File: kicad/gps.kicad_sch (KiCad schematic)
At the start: 61 parts, among them J1 Bus_PCI_Express_x1, J2 USB_C_Receptacle_USB2.0_16P, J3 Conn_01x02, J4 USB_C_Receptacle_USB2.0_16P, U2 W25Q128JVP, U3 MCP25625T-E/ML, U4 RP2040, U5 NEO-M9N, X1 ABM8-272-T3, Y1 X322516MLB4SI

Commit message: Update gps.kicad_pcb
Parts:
- RF1: footprint GPSLIB:SMA-SMD_BWSMA-KE-P001 -> GPSLIB:SMA-TH_BWSMA-KWE-Z001
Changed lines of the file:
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@@
 			)
 		)
-		(property "Footprint" "GPSLIB:SMA-SMD_BWSMA-KE-P001"
+		(property "Footprint" "GPSLIB:SMA-TH_BWSMA-KWE-Z001"
 			(at 316.23 96.52 0)
 			(effects

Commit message: Update footprints
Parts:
- S1, S2: footprint TS-1187A-B-A-B:SW_TS-1187A-B-A-B -> GPSLIB:SW_TS-1187A-B-A-B
- U3: footprint MCP25625T_E_ML:QFN28_6X6MC_MCH -> GPSLIB:QFN28_6X6MC_MCH
- X1: footprint ABM8-272-T3:ABM8-272-T3_ABR -> GPSLIB:ABM8-272-T3_ABR
- Y1: footprint X322516MLB4SI:OSC_X322516MLB4SI -> GPSLIB:OSC_X322516MLB4SI
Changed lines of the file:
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@@
 			)
 		)
-		(property "Footprint" "X322516MLB4SI:OSC_X322516MLB4SI"
+		(property "Footprint" "GPSLIB:OSC_X322516MLB4SI"
 			(at 304.8 231.14 0)
 			(effects
@@
 			)
 		)
-		(property "Footprint" "TS-1187A-B-A-B:SW_TS-1187A-B-A-B"
+		(property "Footprint" "GPSLIB:SW_TS-1187A-B-A-B"
 			(at 48.26 67.31 0)
 			(effects
@@
 			)
 		)
-		(property "Footprint" "ABM8-272-T3:ABM8-272-T3_ABR"
+		(property "Footprint" "GPSLIB:ABM8-272-T3_ABR"
 			(at 45.72 232.41 0)
 			(effects
@@
 			)
 		)
-		(property "Footprint" "MCP25625T_E_ML:QFN28_6X6MC_MCH"
+		(property "Footprint" "GPSLIB:QFN28_6X6MC_MCH"
 			(at 287.02 171.45 0)
 			(effects
@@
 			)
 		)
-		(property "Footprint" "TS-1187A-B-A-B:SW_TS-1187A-B-A-B"
+		(property "Footprint" "GPSLIB:SW_TS-1187A-B-A-B"
 			(at 35.56 189.23 0)
 			(effects

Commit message: wip
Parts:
- added R3, R4: 27, Resistor_SMD:R_0402_1005Metric, symbol Device:R
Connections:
- net GPS_USB_D+: now also R4.1; no longer U5.6 (USB_DP)
- net GPS_USB_D-: now also R3.1; no longer U5.5 (USB_DM)
- new net: R3.2, U5.5 (USB_DM)
- new net: R4.2, U5.6 (USB_DP)

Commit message: Update pcb
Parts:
- R10, R13: value 150 -> 1k; JLC Link https://jlcpcb.com/partdetail/23535-0603WAF1500T5E/C22808 -> (none); LCSC Part # C22808 -> (none); info 150 ohm -> (none)
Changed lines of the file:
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@@
 			)
 		)
-		(property "Value" "150"
+		(property "Value" "1k"
 			(at 266.446 251.46 0)
 			(effects
@@
 			)
 		)
-		(property "JLC Link" "https://jlcpcb.com/partdetail/23535-0603WAF1500T5E/C22808"
+		(property "JLC Link" ""
 			(at 271.78 250.19 0)
 			(effects
@@
 			)
 		)
-		(property "LCSC Part #" "C22808"
+		(property "LCSC Part #" ""
 			(at 271.78 250.19 0)
 			(effects
@@
 			)
 		)
-		(property "info" "150 ohm"
+		(property "info" ""
 			(at 271.78 250.19 0)
 			(effects
@@
 			)
 		)
-		(property "Value" "150"
+		(property "Value" "1k"
 			(at 253.746 251.46 0)
 			(effects
@@
 			)
 		)
-		(property "JLC Link" "https://jlcpcb.com/partdetail/23535-0603WAF1500T5E/C22808"
+		(property "JLC Link" ""
 			(at 259.08 250.19 0)
 			(effects
@@
 			)
 		)
-		(property "LCSC Part #" "C22808"
+		(property "LCSC Part #" ""
 			(at 259.08 250.19 0)
 			(effects
@@
 			)
 		)
-		(property "info" "150 ohm"
+		(property "info" ""
 			(at 259.08 250.19 0)
 			(effects

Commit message: Update pcb
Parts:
- R20, R22: LCSC Part # C25105 -> (none); info 1000 ohm -> (none)
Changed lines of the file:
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@@
 			)
 		)
-		(property "LCSC Part #" "C25105"
+		(property "LCSC Part #" ""
 			(at 384.81 143.51 0)
 			(effects
@@
 			)
 		)
-		(property "info" "1000 ohm"
+		(property "info" ""
 			(at 384.81 143.51 0)
 			(effects
@@
 			)
 		)
-		(property "LCSC Part #" "C25105"
+		(property "LCSC Part #" ""
 			(at 377.19 143.51 0)
 			(effects
@@
 			)
 		)
-		(property "info" "1000 ohm"
+		(property "info" ""
 			(at 377.19 143.51 0)
 			(effects

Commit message: Update pcb
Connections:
- net +3.3V: now also C22.1, U5.23 (VCC)
- net +3V3: no longer C22.1, U5.23 (VCC)
- net RF_ANT: now reaches L1.2, RF1.5, U5.11 (RF_IN)
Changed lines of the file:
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@@
 		)
 	)
+	(global_label "RF_ANT"
+		(shape input)
+		(at 294.64 96.52 90)
+		(fields_autoplaced yes)
+		(effects
+			(font
+				(size 1.27 1.27)
+			)
+			(justify left)
+		)
+		(property "Intersheetrefs" "${INTERSHEET_REFS}"
+			(at 294.64 86.8219 90)
+			(effects
+				(font
+					(size 1.27 1.27)
+				)
+				(justify left)
+				(hide yes)
+			)
+		)
+	)
 	(global_label "CANSTBY"
 		(shape input)
@@
 	)
 	(symbol
-		(lib_id "power:+3V3")
-		(at 260.35 71.12 0)
-		(unit 1)
-		(exclude_from_sim no)
-		(in_bom yes)
-		(on_board yes)
-		(dnp no)
-		(fields_autoplaced yes)
-		(property "Reference" "#PWR057"
-			(at 260.35 74.93 0)
-			(effects
-				(font
-					(size 1.27 1.27)
-				)
-				(hide yes)
-			)
-		)
-		(property "Value" "+3V3"
-			(at 260.35 66.04 0)
-			(effects
-				(font
-					(size 1.27 1.27)
-				)
-			)
-		)
-		(property "Footprint" ""
-			(at 260.35 71.12 0)
-			(effects
-				(font
-					(size 1.27 1.27)
-				)
-				(hide yes)
-			)
-		)
-		(property "Datasheet" ""
-			(at 260.35 71.12 0)
-			(effects
-				(font
-					(size 1.27 1.27)
-				)
-				(hide yes)
-			)
-		)
-		(property "Description" ""
-			(at 260.35 71.12 0)
-			(effects
-				(font
-					(size 1.27 1.27)
-				)
-				(hide yes)
-			)
-		)
-		(pin "1"
-		)
-		(instances
-			(project "gps"
-				(path "/e1ff46b9-0cf9-4507-8034-1e95fc3013fc"
-					(reference "#PWR057")
-					(unit 1)
-				)
-			)
-		)
-	)
-	(symbol
 		(lib_id "power:GND")
 		(at 133.35 242.57 90)
@@
 	)
 	(symbol
-		(lib_id "power:+3V3")
-		(at 237.49 59.69 0)
+		(lib_id "power:GND")
+		(at 313.69 238.76 0)
 		(unit 1)
 		(exclude_from_sim no)
@@
 		(dnp no)
 		(fields_autoplaced yes)
-		(property "Reference" "#PWR055"
-			(at 237.49 63.5 0)
+		(property "Reference" "#PWR051"
+			(at 313.69 245.11 0)
 			(effects
 				(font
@@
 			)
 		)
-		(property "Value" "+3V3"
-			(at 237.49 54.61 0)
+		(property "Value" "GND"
+			(at 313.69 243.84 0)
 			(effects
 				(font
 					(size 1.27 1.27)
 				)
+				(hide yes)
 			)
 		)
 		(property "Footprint" ""
-			(at 237.49 59.69 0)
+			(at 313.69 238.76 0)
 			(effects
 				(font
@@
 		)
 		(property "Datasheet" ""
-			(at 237.49 59.69 0)
+			(at 313.69 238.76 0)
 			(effects
 				(font
@@
 			)
 		)
-		(property "Description" ""
-			(at 237.49 59.69 0)
+		(property "Description" "Power symbol creates a global label with name \"GND\" , ground"
+			(at 313.69 238.76 0)
 			(effects
 				(font
@@
 			(project "gps"
 				(path "/e1ff46b9-0cf9-4507-8034-1e95fc3013fc"
-					(reference "#PWR055")
+					(reference "#PWR051")
 					(unit 1)
 				)
@@
 	)
 	(symbol
-		(lib_id "power:GND")
-		(at 313.69 238.76 0)
+		(lib_id "power:+3.3V")
+		(at 237.49 59.69 0)
 		(unit 1)
 		(exclude_from_sim no)
@@
 		(on_board yes)
 		(dnp no)
-		(fields_autoplaced yes)
-		(property "Reference" "#PWR051"
-			(at 313.69 245.11 0)
+		(property "Reference" "#PWR055"
+			(at 237.49 63.5 0)
 			(effects
 				(font
@@
 			)
 		)
-		(property "Value" "GND"
-			(at 313.69 243.84 0)
+		(property "Value" "+3.3V"
+			(at 237.49 54.61 0)
 			(effects
 				(font
 					(size 1.27 1.27)
 				)
-				(hide yes)
 			)
 		)
 		(property "Footprint" ""
-			(at 313.69 238.76 0)
+			(at 237.49 59.69 0)
 			(effects
 				(font
@@
 		)
 		(property "Datasheet" ""
-			(at 313.69 238.76 0)
+			(at 237.49 59.69 0)
 			(effects
 				(font
@@
 			)
 		)
-		(property "Description" "Power symbol creates a global label with name \"GND\" , ground"
-			(at 313.69 238.76 0)
+		(property "Description" "Power symbol creates a global label with name \"+3.3V\""
+			(at 237.49 59.69 0)
 			(effects
 				(font
@@
 			(project "gps"
 				(path "/e1ff46b9-0cf9-4507-8034-1e95fc3013fc"
-					(reference "#PWR051")
+					(reference "#PWR055")
 					(unit 1)
 				)
@@
 					(unit 1)
 				)
+			)
+		)
+	)
+	(symbol
+		(lib_id "power:+3.3V")
+		(at 260.35 71.12 0)
+		(unit 1)
+		(exclude_from_sim no)
+		(in_bom yes)
+		(on_board yes)
+		(dnp no)
+		(property "Reference" "#PWR057"
+			(at 260.35 74.93 0)
+			(effects
+				(font
+					(size 1.27 1.27)
+				)
+				(hide yes)
+			)
+		)
+		(property "Value" "+3.3V"
+			(at 260.35 66.04 0)
+			(effects
+				(font
+					(size 1.27 1.27)
+				)
+			)
+		)
+		(property "Footprint" ""
+			(at 260.35 71.12 0)
+			(effects
+				(font
+					(size 1.27 1.27)
+				)
+				(hide yes)
+			)
+		)
+		(property "Datasheet" ""
+			(at 260.35 71.12 0)
+			(effects
+				(font
+					(size 1.27 1.27)
+				)
+				(hide yes)
+			)
+		)
+		(property "Description" "Power symbol creates a global label with name \"+3.3V\""
+			(at 260.35 71.12 0)
+			(effects
+				(font
+					(size 1.27 1.27)
+				)
+				(hide yes)
+			)
+		)
+		(pin "1"
+		)
+		(instances
+			(project "gps"
+				(path "/e1ff46b9-0cf9-4507-8034-1e95fc3013fc"
+					(reference "#PWR057")
+					(unit 1)
+				)

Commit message: Update pcb
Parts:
- removed B1: 6.8MM_COIN_CELL, GPSLIB:6.8mm-coincell-ML414H_IV01E, symbol SparkFun u-blox GNSS MAX-M10S-eagle-import:ML414H_IV01E_BATTERY
- added BAT1: 2998, BAT-SMD_C238096, symbol gpsmodule:2998
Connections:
- net +3V3 is gone; now on net +3.3V: PWR1.2
- net 3.3V is gone; now on net +3.3V: D2.A
- net BACKUP: now also BAT1.1 (+), BAT1.2 (+)
- net GND: now also BAT1.3 (-)
- net U4_USB_D+: now reaches R16.2, U4.47 (USB_DP)
- net U4_USB_D-: now reaches R17.2, U4.46 (USB_DM)
- net U5_USB_D+: now reaches R3.2, U5.5 (USB_DM)
- net U5_USB_D-: now reaches R4.2, U5.6 (USB_DP)

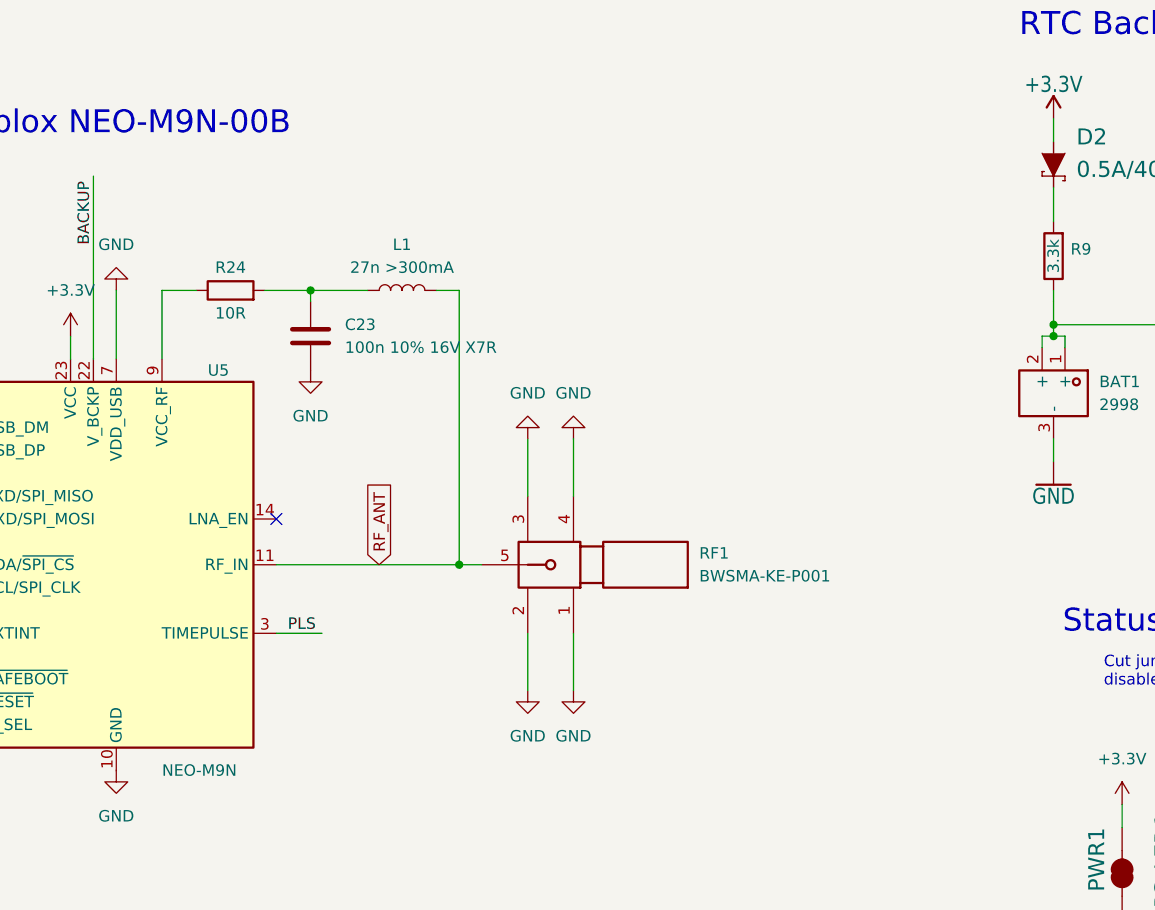
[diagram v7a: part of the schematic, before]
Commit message: Add MOSFET bias-tee switch for active GPS antenna
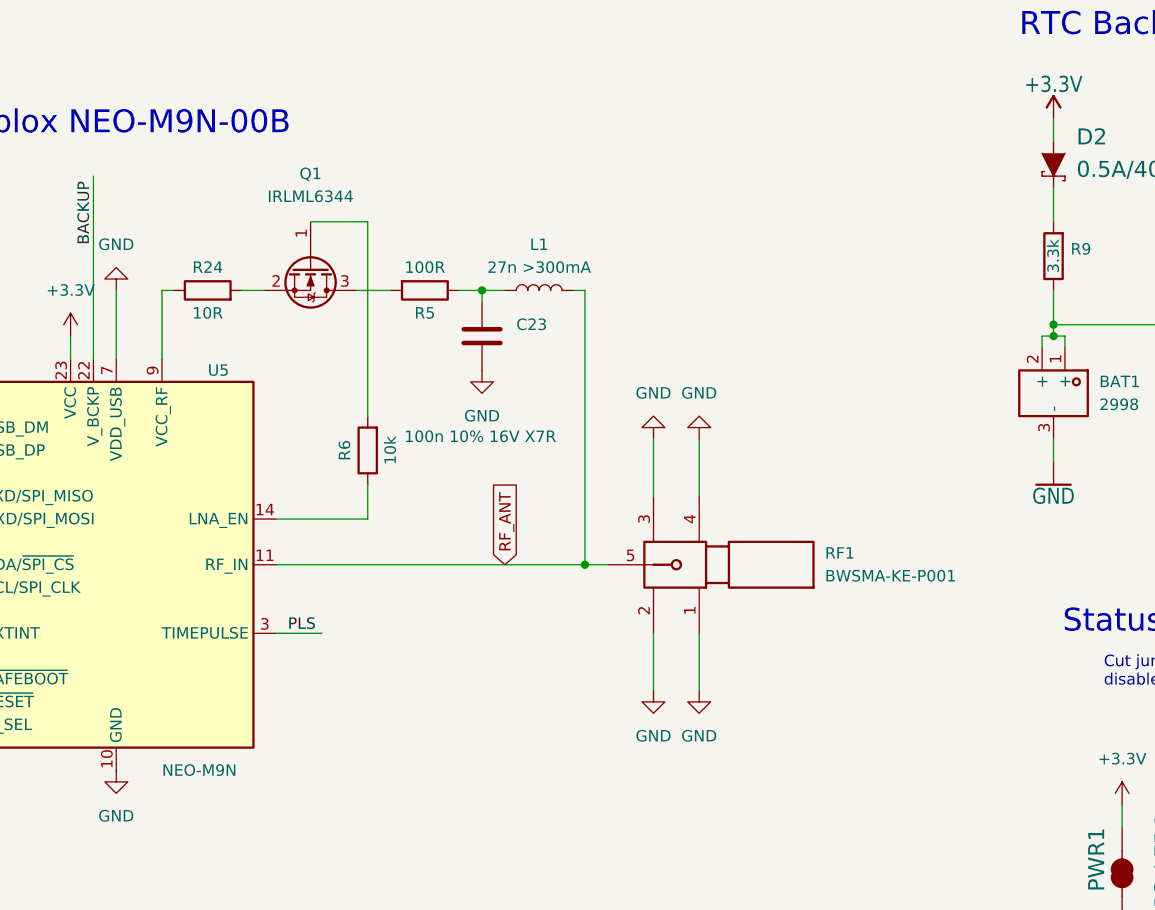
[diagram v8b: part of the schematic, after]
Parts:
- added Q1: IRLML6344, Package_TO_SOT_SMD:SOT-23, symbol Transistor_FET:IRLML6244
- added R5: 100R, Resistor_SMD:R_0402_1005Metric, symbol Device:R
- added R6: 10k, Resistor_SMD:R_0402_1005Metric, symbol Device:R
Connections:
- net at U5.14 (LNA_EN): now also R6.1
- net at C23.1, L1.1: now also R5.1; no longer R24.2
- new net: Q1.1 (G), R6.2
- new net: Q1.2 (S), R24.2
- new net: Q1.3 (D), R5.2
- no-connect marks 45 -> 44
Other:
- moved on the sheet: C23, L1, R24, RF1
